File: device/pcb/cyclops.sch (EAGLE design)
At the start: 184 parts, among them Q1 NDS351AN, Q2 NDS351AN, Q3 NDS351AN, Q4 IRF510, U1 MCP4921, U10 ADG1201, U11 THS4281, U12 MAX4564, U13 ZXTD, U14 ZXTD, U15 OPA1664, U16 LTM8020, U2 LT1931, U3 LT1764A, U4 BD00FC0WEFJ, U5 TPS72325, U6 LT1711, U7 TLV3701, U8 ADR03, U9 LT1880

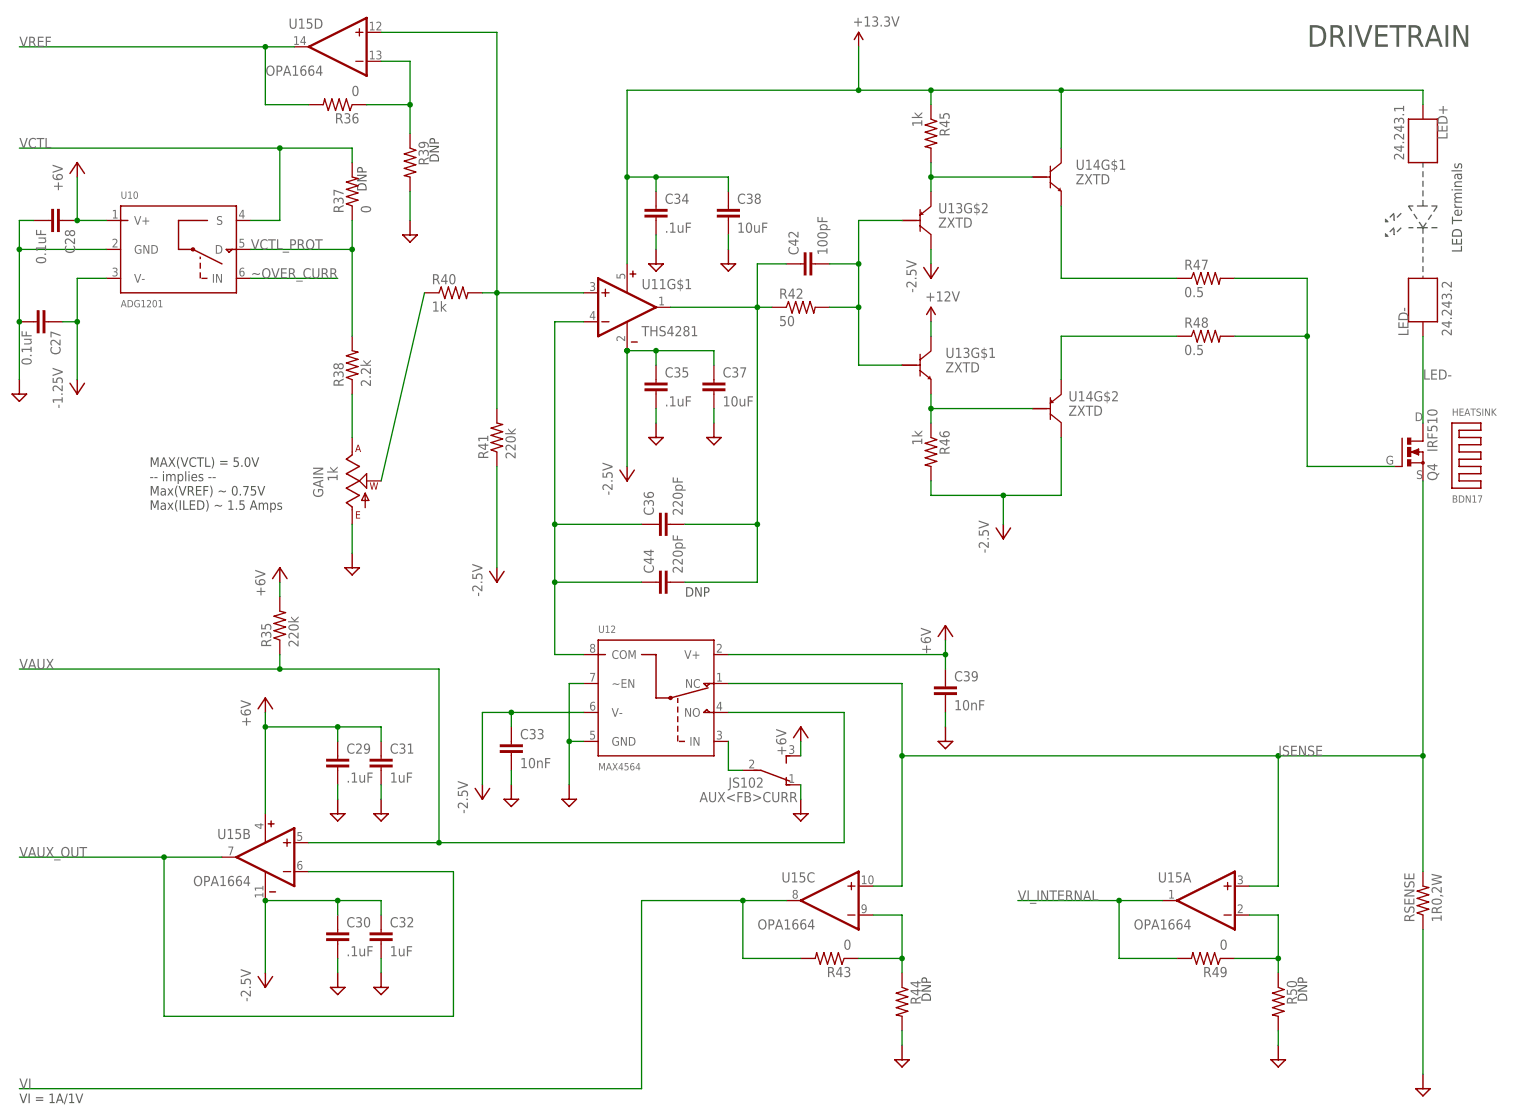
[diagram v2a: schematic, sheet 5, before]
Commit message: Added bandwidth limit selection
- Added analog switch to insert 6.8nF of compensation capacitance into
  the current sense feedback loop for when people use long cables or
  slow transimpedance photodiode amplifiers
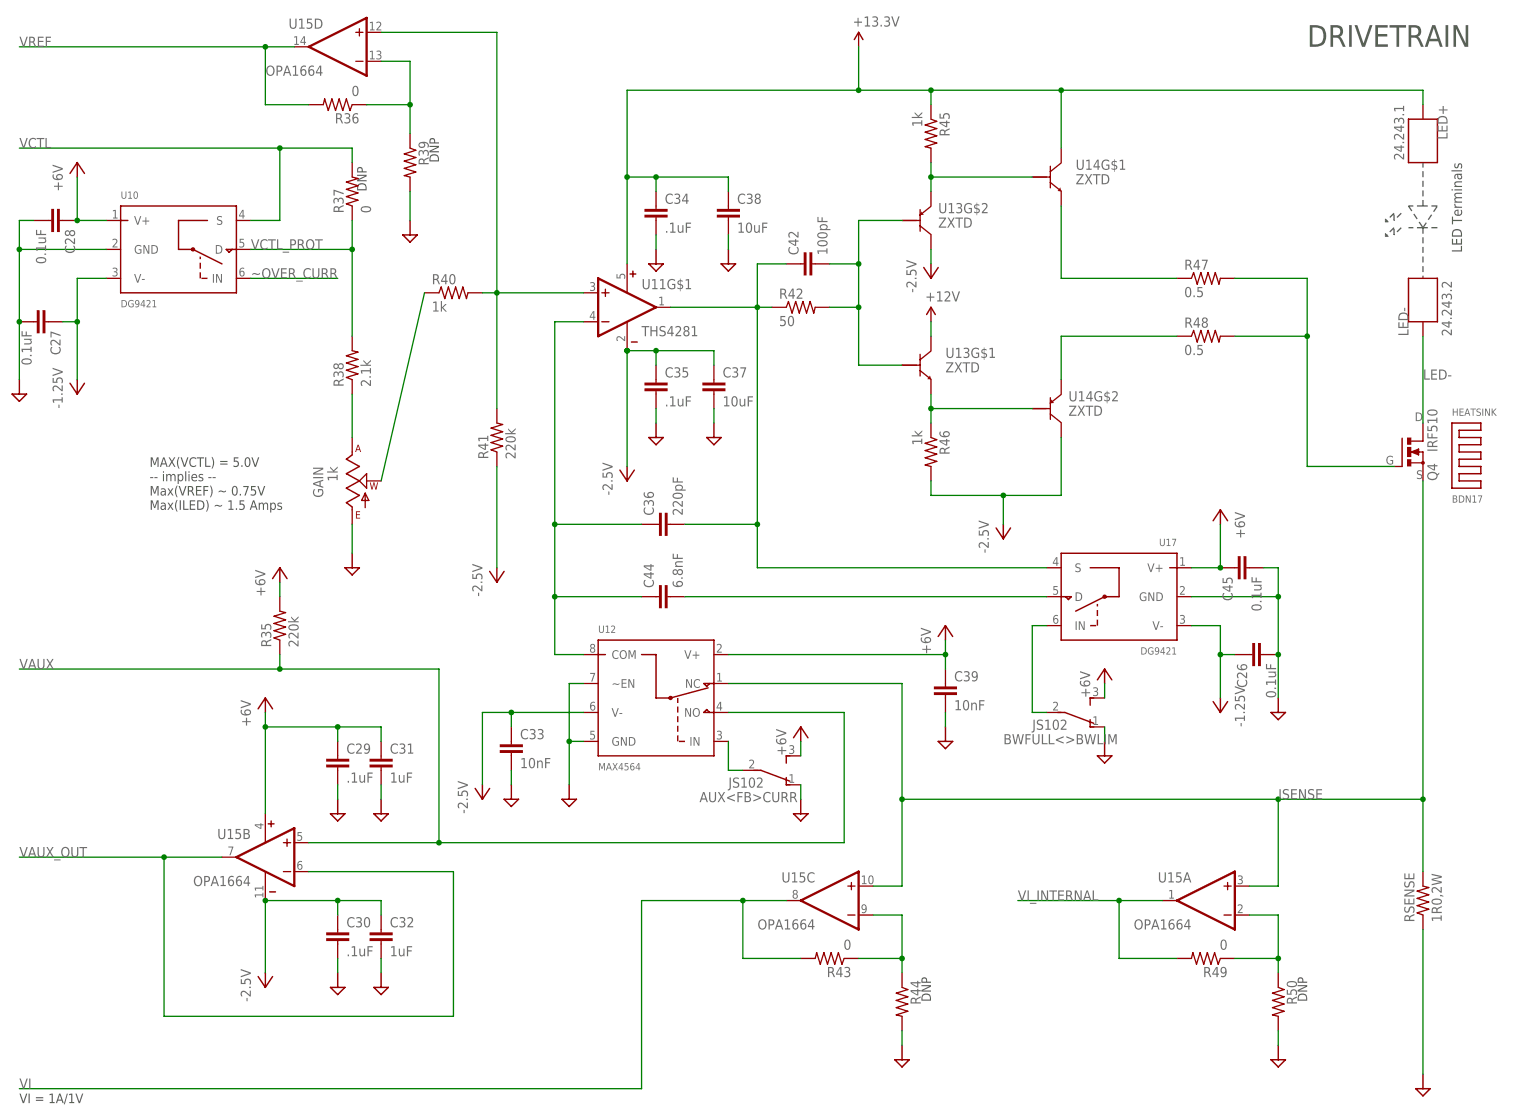
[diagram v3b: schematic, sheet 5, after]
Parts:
- added BWFULL<>BWLIM: JS102, cyclops:SPDT_JS
- added C26, C45: 0.1uF, cyclops:C_0603
- added U17: DG9421, jonnew:SPST_IC_SOT23-6
- C44: value 220pF -> 6.8nF
- R38: value 2.2k -> 2.1k
- U10: value ADG1201 -> DG9421
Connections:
- new net IN1: BWFULL<>BWLIM.2, U17.IN
- new net N$40: C44.2, U17.D
- net +6V: now also BWFULL<>BWLIM.3, C45.1, U17.V+
- net -2.5V: now also C26.1, U17.V-
- net GND: now also BWFULL<>BWLIM.1, C26.2, C45.2, U17.GND
- net N$13: now also U17.S; no longer C44.2
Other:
- moved on the sheet: C44
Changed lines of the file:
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@@
 <?xml version="1.0" encoding="utf-8"?>
 <!DOCTYPE eagle SYSTEM "eagle.dtd">
-<eagle version="6.5.0">
+<eagle version="6.6.0">
 <drawing>
 <settings>
@@
 <part name="U$42" library="cyclops" deviceset="GND2" device=""/>
 <part name="U$43" library="cyclops" deviceset="GND2" device=""/>
-<part name="R38" library="cyclops" deviceset="R" device="_0603" value="2.2k"/>
+<part name="R38" library="cyclops" deviceset="R" device="_0603" value="2.1k"/>
 <part name="LED-" library="cyclops" deviceset="BANANA_TO_BOARD" device="_A2107" value="24.243.2"/>
 <part name="LED+" library="cyclops" deviceset="BANANA_TO_BOARD" device="_A2107" value="24.243.1"/>
@@
 <part name="P+1" library="jonnew" deviceset="+5V" device="" value="+6V"/>
 <part name="P+5" library="jonnew" deviceset="+5V" device="" value="+6V"/>
-<part name="U10" library="jonnew" deviceset="SPST_IC" device="_SOT23-6" value="ADG1201"/>
+<part name="U10" library="jonnew" deviceset="SPST_IC" device="_SOT23-6" value="DG9421"/>
 <part name="P+9" library="jonnew" deviceset="+5V" device="" value="+6V"/>
 <part name="P+10" library="jonnew" deviceset="+5V" device="" value="+6V"/>
@@
 <part name="R42" library="cyclops" deviceset="R" device="_0603" value="50"/>
 <part name="C42" library="cyclops" deviceset="C" device="_0603" value="100pF"/>
-<part name="C44" library="cyclops" deviceset="C" device="_0603" value="220pF"/>
+<part name="C44" library="cyclops" deviceset="C" device="_0603" value="6.8nF"/>
+<part name="C26" library="cyclops" deviceset="C" device="_0603" value="0.1uF"/>
+<part name="C45" library="cyclops" deviceset="C" device="_0603" value="0.1uF"/>
+<part name="U$9" library="cyclops" deviceset="GND2" device=""/>
+<part name="P-9" library="cyclops" deviceset="-5V" device="" value="-1.25V"/>
+<part name="P+21" library="jonnew" deviceset="+5V" device="" value="+6V"/>
+<part name="U17" library="jonnew" deviceset="SPST_IC" device="_SOT23-6" value="DG9421"/>
+<part name="BWFULL&lt;&gt;BWLIM" library="cyclops" deviceset="SPDT" device="_JS" value="JS102"/>
+<part name="U$45" library="cyclops" deviceset="GND2" device=""/>
+<part name="P+22" library="jonnew" deviceset="+5V" device="" value="+6V"/>
 </parts>
 <sheets>
@@
 <text x="-7.62" y="124.46" size="1.6764" layer="97" rot="R90">DNP</text>
 <text x="-20.32" y="119.38" size="1.6764" layer="97" rot="R90">DNP</text>
-<text x="35.56" y="48.26" size="1.6764" layer="97">DNP</text>
 </plain>
 <instances>
@@
 <instance part="R42" gate="R" x="55.88" y="99.06"/>
 <instance part="C42" gate="C" x="55.88" y="106.68" rot="R90"/>
-<instance part="C44" gate="C" x="30.48" y="50.8" rot="R90"/>
+<instance part="C44" gate="C" x="30.48" y="48.26" rot="R90"/>
+<instance part="C26" gate="C" x="134.62" y="38.1" rot="MR270"/>
+<instance part="C45" gate="C" x="132.08" y="53.34" rot="MR270"/>
+<instance part="U$9" gate="G$1" x="139.7" y="27.94" rot="MR0"/>
+<instance part="P-9" gate="1" x="129.54" y="27.94" rot="MR0"/>
+<instance part="P+21" gate="1" x="129.54" y="63.5" rot="MR0"/>
+<instance part="U17" gate="G$1" x="111.76" y="45.72" rot="MR0"/>
+<instance part="BWFULL&lt;&gt;BWLIM" gate="G$1" x="101.6" y="27.94" smashed="yes" rot="MR180">
+<attribute name="NAME" x="91.44" y="24.13" size="1.778" layer="95" rot="MR180"/>
+<attribute name="VALUE" x="96.52" y="26.67" size="1.778" layer="96" rot="MR180"/>
+</instance>
+<instance part="U$45" gate="G$1" x="109.22" y="20.32"/>
+<instance part="P+22" gate="1" x="109.22" y="35.56"/>
 </instances>
 <busses>
@@
 <wire x1="139.7" y1="-27.94" x2="139.7" y2="-30.48" width="0.1524" layer="91"/>
 </segment>
+<segment>
+<pinref part="C26" gate="C" pin="2"/>
+<wire x1="139.7" y1="48.26" x2="124.46" y2="48.26" width="0.1524" layer="91"/>
+<wire x1="139.7" y1="48.26" x2="139.7" y2="38.1" width="0.1524" layer="91"/>
+<junction x="139.7" y="38.1"/>
+<wire x1="139.7" y1="38.1" x2="139.7" y2="30.48" width="0.1524" layer="91"/>
+<pinref part="U17" gate="G$1" pin="GND"/>
+<wire x1="139.7" y1="48.26" x2="139.7" y2="53.34" width="0.1524" layer="91"/>
+<junction x="139.7" y="48.26"/>
+<pinref part="C45" gate="C" pin="2"/>
+<wire x1="139.7" y1="53.34" x2="137.16" y2="53.34" width="0.1524" layer="91"/>
+</segment>
+<segment>
+<pinref part="BWFULL&lt;&gt;BWLIM" gate="G$1" pin="1"/>
+<wire x1="109.22" y1="25.4" x2="109.22" y2="22.86" width="0.1524" layer="91"/>
+</segment>
 </net>
 <net name="+13.3V" class="1">
@@
 <wire x1="-71.12" y1="104.14" x2="-71.12" y2="96.52" width="0.1524" layer="91"/>
 </segment>
+<segment>
+<pinref part="C26" gate="C" pin="1"/>
+<wire x1="132.08" y1="38.1" x2="129.54" y2="38.1" width="0.1524" layer="91"/>
+<wire x1="129.54" y1="30.48" x2="129.54" y2="38.1" width="0.1524" layer="91"/>
+<junction x="129.54" y="38.1"/>
+<pinref part="U17" gate="G$1" pin="V-"/>
+<wire x1="124.46" y1="43.18" x2="129.54" y2="43.18" width="0.1524" layer="91"/>
+<wire x1="129.54" y1="43.18" x2="129.54" y2="38.1" width="0.1524" layer="91"/>
+</segment>
 </net>
 <net name="VCTL_PROTECT" class="0">
@@
 <pinref part="C42" gate="C" pin="1"/>
 <wire x1="48.26" y1="106.68" x2="53.34" y2="106.68" width="0.1524" layer="91"/>
-<pinref part="C44" gate="C" pin="2"/>
-<wire x1="35.56" y1="50.8" x2="48.26" y2="50.8" width="0.1524" layer="91"/>
-<wire x1="48.26" y1="50.8" x2="48.26" y2="60.96" width="0.1524" layer="91"/>
+<pinref part="U17" gate="G$1" pin="S"/>
+<wire x1="99.06" y1="53.34" x2="48.26" y2="53.34" width="0.1524" layer="91"/>
+<wire x1="48.26" y1="53.34" x2="48.26" y2="60.96" width="0.1524" layer="91"/>
 <junction x="48.26" y="60.96"/>
 </segment>
@@
 <wire x1="12.7" y1="96.52" x2="12.7" y2="60.96" width="0.1524" layer="91"/>
 <pinref part="U12" gate="G$1" pin="COM"/>
-<wire x1="12.7" y1="60.96" x2="12.7" y2="50.8" width="0.1524" layer="91"/>
-<wire x1="12.7" y1="50.8" x2="12.7" y2="38.1" width="0.1524" layer="91"/>
+<wire x1="12.7" y1="60.96" x2="12.7" y2="48.26" width="0.1524" layer="91"/>
+<wire x1="12.7" y1="48.26" x2="12.7" y2="38.1" width="0.1524" layer="91"/>
 <wire x1="12.7" y1="38.1" x2="17.78" y2="38.1" width="0.1524" layer="91"/>
 <pinref part="C36" gate="C" pin="1"/>
@@
 <junction x="12.7" y="60.96"/>
 <pinref part="C44" gate="C" pin="1"/>
-<wire x1="27.94" y1="50.8" x2="12.7" y2="50.8" width="0.1524" layer="91"/>
-<junction x="12.7" y="50.8"/>
+<wire x1="27.94" y1="48.26" x2="12.7" y2="48.26" width="0.1524" layer="91"/>
+<junction x="12.7" y="48.26"/>
 </segment>
 </net>
@@
 <junction x="-38.1" y="25.4"/>
 </segment>
+<segment>
+<pinref part="C45" gate="C" pin="1"/>
+<pinref part="U17" gate="G$1" pin="V+"/>
+<wire x1="124.46" y1="53.34" x2="129.54" y2="53.34" width="0.1524" layer="91"/>
+<junction x="129.54" y="53.34"/>
+<wire x1="129.54" y1="60.96" x2="129.54" y2="53.34" width="0.1524" layer="91"/>
+</segment>
+<segment>
+<pinref part="BWFULL&lt;&gt;BWLIM" gate="G$1" pin="3"/>
+<wire x1="109.22" y1="30.48" x2="109.22" y2="33.02" width="0.1524" layer="91"/>
+</segment>
 </net>
 <net name="LED-" class="0">
@@
 <net name="ISENSE" class="0">
 <segment>
-<wire x1="165.1" y1="20.32" x2="165.1" y2="0" width="0.1524" layer="91"/>
+<wire x1="165.1" y1="12.7" x2="165.1" y2="0" width="0.1524" layer="91"/>
 <wire x1="68.58" y1="-2.54" x2="73.66" y2="-2.54" width="0.1524" layer="91"/>
-<wire x1="73.66" y1="-2.54" x2="73.66" y2="20.32" width="0.1524" layer="91"/>
+<wire x1="73.66" y1="-2.54" x2="73.66" y2="12.7" width="0.1524" layer="91"/>
 <pinref part="U15" gate="C" pin="+IN"/>
 <pinref part="RSENSE" gate="R" pin="2"/>
-<wire x1="73.66" y1="20.32" x2="139.7" y2="20.32" width="0.1524" layer="91"/>
-<wire x1="139.7" y1="20.32" x2="165.1" y2="20.32" width="0.1524" layer="91"/>
+<wire x1="73.66" y1="12.7" x2="139.7" y2="12.7" width="0.1524" layer="91"/>
+<wire x1="139.7" y1="12.7" x2="165.1" y2="12.7" width="0.1524" layer="91"/>
 <wire x1="43.18" y1="33.02" x2="73.66" y2="33.02" width="0.1524" layer="91"/>
-<wire x1="73.66" y1="33.02" x2="73.66" y2="20.32" width="0.1524" layer="91"/>
-<junction x="73.66" y="20.32"/>
+<wire x1="73.66" y1="33.02" x2="73.66" y2="12.7" width="0.1524" layer="91"/>
+<junction x="73.66" y="12.7"/>
 <pinref part="U12" gate="G$1" pin="NC"/>
 <wire x1="134.62" y1="-2.54" x2="139.7" y2="-2.54" width="0.1524" layer="91"/>
-<wire x1="139.7" y1="-2.54" x2="139.7" y2="20.32" width="0.1524" layer="91"/>
-<junction x="139.7" y="20.32"/>
+<wire x1="139.7" y1="-2.54" x2="139.7" y2="12.7" width="0.1524" layer="91"/>
+<junction x="139.7" y="12.7"/>
 <pinref part="U15" gate="A" pin="+IN"/>
-<label x="139.7" y="20.32" size="1.778" layer="95"/>
+<label x="139.7" y="12.7" size="1.778" layer="95"/>
 <pinref part="Q4" gate="G$1" pin="S"/>
-<wire x1="165.1" y1="68.58" x2="165.1" y2="20.32" width="0.1524" layer="91"/>
-<junction x="165.1" y="20.32"/>
+<wire x1="165.1" y1="68.58" x2="165.1" y2="12.7" width="0.1524" layer="91"/>
+<junction x="165.1" y="12.7"/>
 </segment>
 </net>
@@
 </segment>
 </net>
+<net name="N$40" class="0">
+<segment>
+<pinref part="C44" gate="C" pin="2"/>
+<pinref part="U17" gate="G$1" pin="D"/>
+<wire x1="99.06" y1="48.26" x2="35.56" y2="48.26" width="0.1524" layer="91"/>
+</segment>
+</net>
+<net name="IN1" class="0">
+<segment>
+<pinref part="BWFULL&lt;&gt;BWLIM" gate="G$1" pin="2"/>
+<wire x1="99.06" y1="27.94" x2="96.52" y2="27.94" width="0.1524" layer="91"/>
+<pinref part="U17" gate="G$1" pin="IN"/>
+<wire x1="99.06" y1="43.18" x2="96.52" y2="43.18" width="0.1524" layer="91"/>
+<wire x1="96.52" y1="43.18" x2="96.52" y2="27.94" width="0.1524" layer="91"/>
+</segment>
+</net>
